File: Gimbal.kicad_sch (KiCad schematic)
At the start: 46 parts, among them J1 XT60-M, J2 USB_C_Receptacle_USB2.0, J3 0022232041, J4 0022232041, J5 0022232041, J6 Conn_01x02, SW1 SW_Push, SW2 SW_Push, U1 ESP32-S2-SOLO, U2 BMI088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

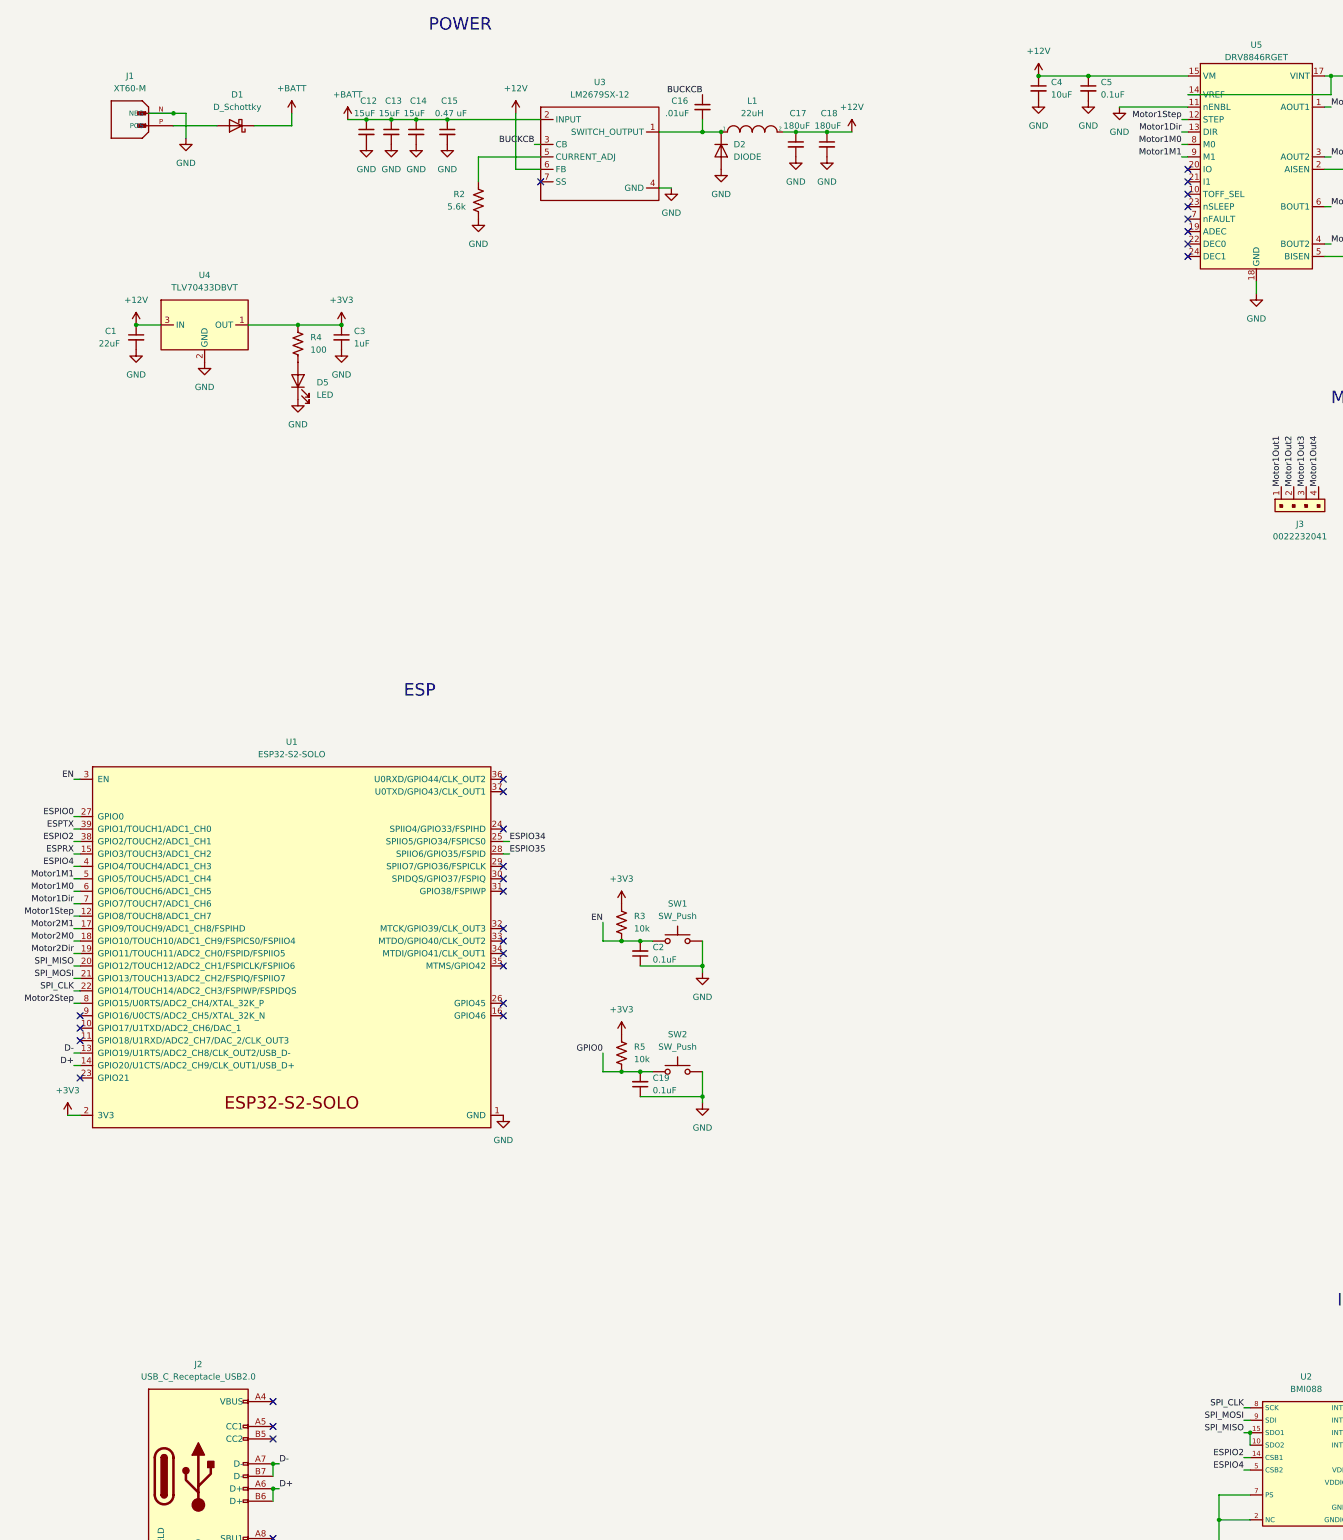
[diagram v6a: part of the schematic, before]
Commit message: fixing schematic erc issues and adding test points
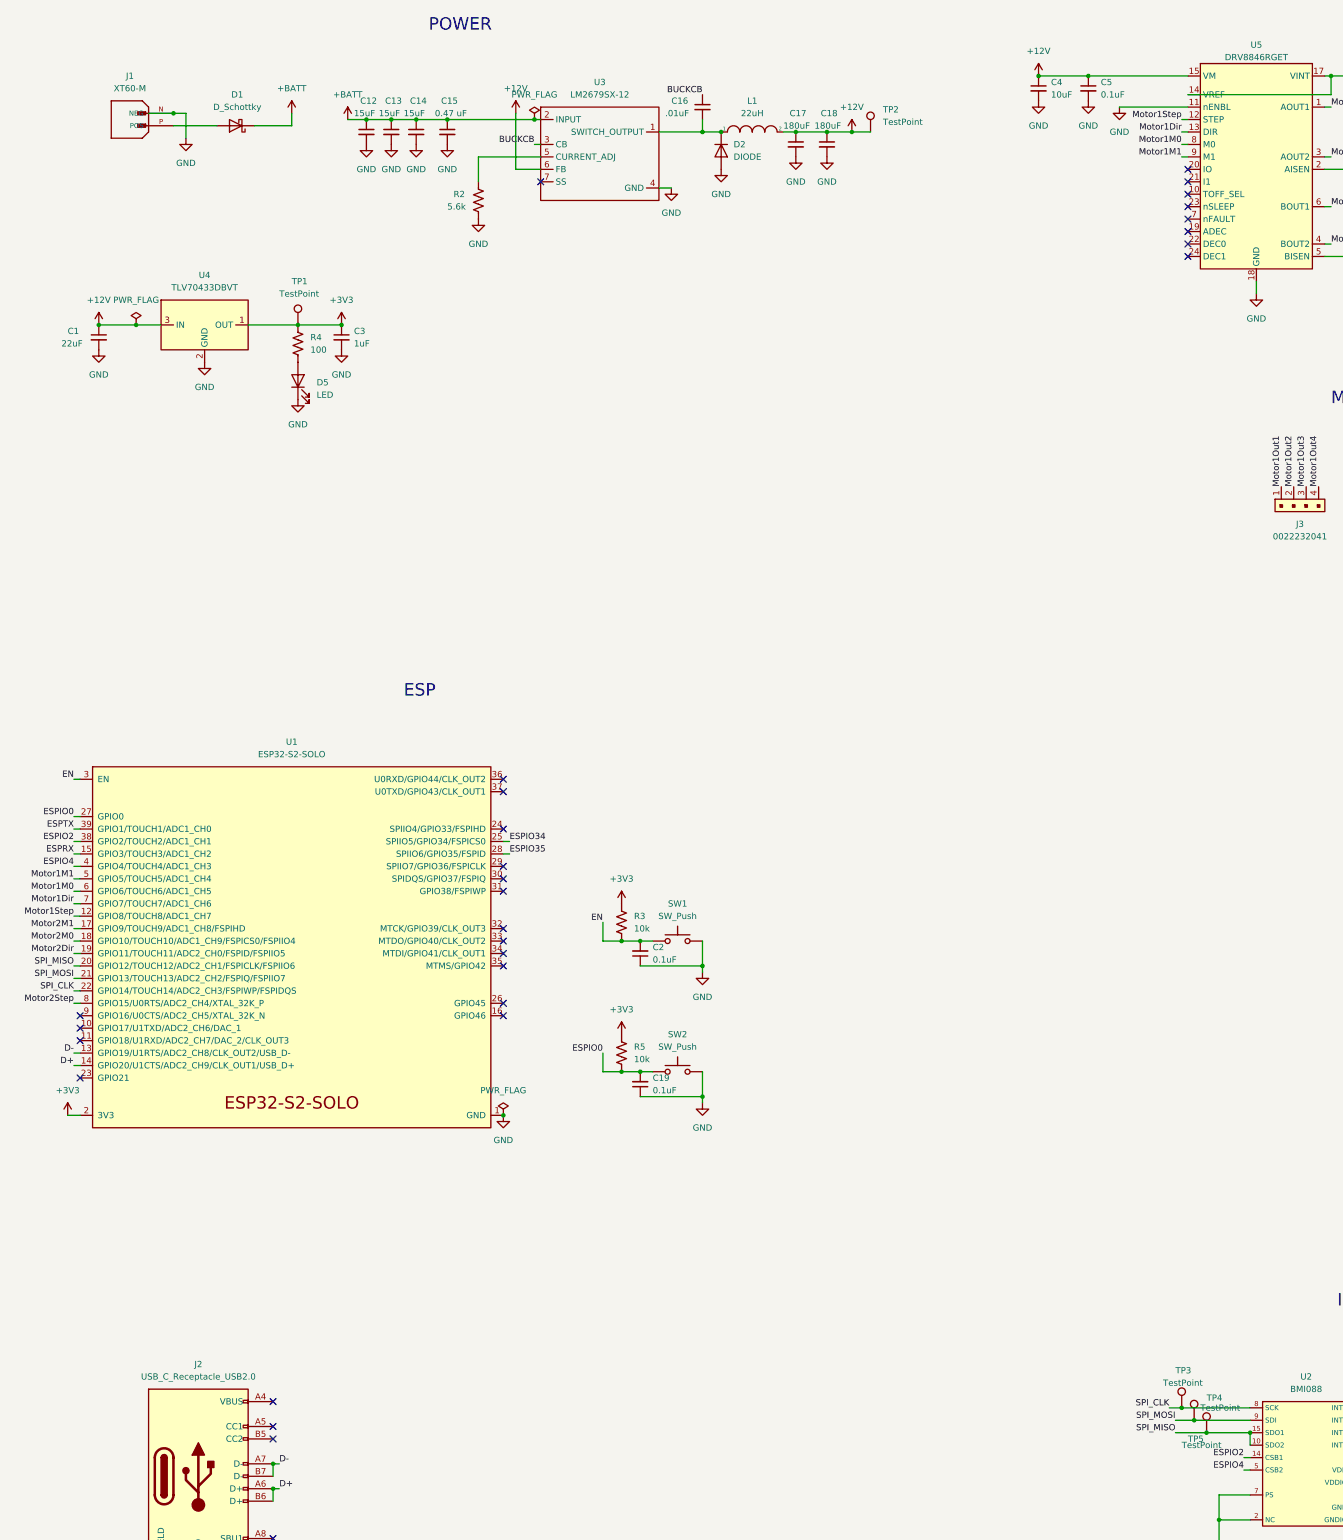
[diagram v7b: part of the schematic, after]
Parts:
- added TP1, TP2, TP3, TP4, TP5: TestPoint, symbol Connector:TestPoint
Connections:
- net GPIO0 is gone; now on net ESPIO0: C19.2, R5.2, SW2.1
- net +12V: now also TP2.1
- net +3V3: now also TP1.1
- net SPI_CLK: now also TP3.1
- net SPI_MISO: now also TP5.1
- net SPI_MOSI: now also TP4.1
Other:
- moved on the sheet: C1
